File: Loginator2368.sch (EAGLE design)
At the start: 69 parts, among them J001 USBSMD, J002 M01PTH, J301 JST 2mm, J401 M06, J402 M04, J403 M10, J404 M06, J406 M12PTH, J701 MICROSD-SOCKET, Q050 PMOS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

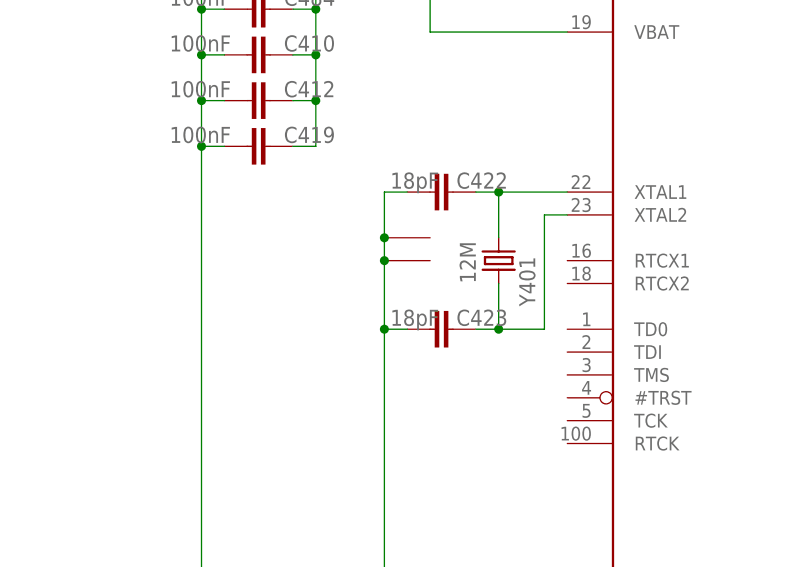
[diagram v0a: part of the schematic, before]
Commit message: Merged Mio's KwanSystems.lbr, updated all eagle files to use it.
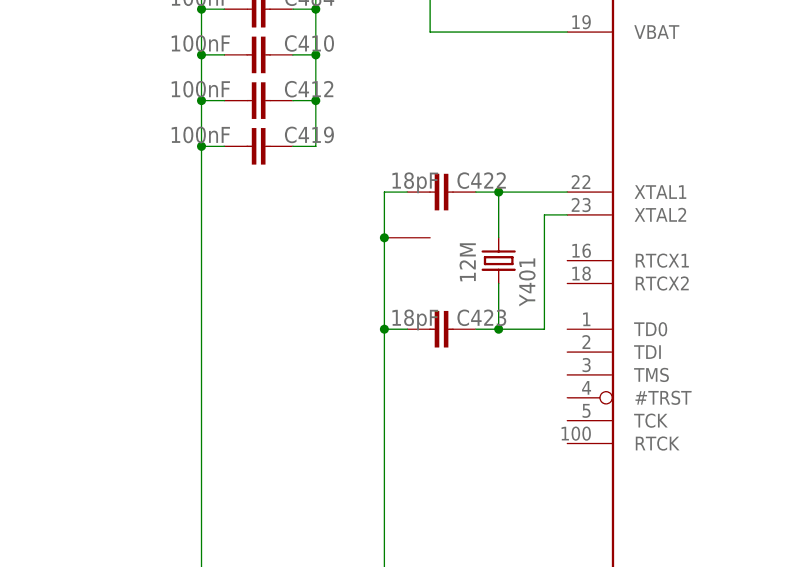
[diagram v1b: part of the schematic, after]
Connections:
- net GND: no longer Y401G$2.1
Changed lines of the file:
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@@
 <?xml version="1.0" encoding="utf-8"?>
 <!DOCTYPE eagle SYSTEM "eagle.dtd">
-<eagle version="6.1">
+<eagle version="6.2">
 <drawing>
 <settings>
@@
 <attribute name="DIGIKEY" value="887-1316-1-ND" x="-233.68" y="220.98" size="1.778" layer="96" rot="R90" display="off"/>
 </instance>
-<instance part="Y401" gate="G$2" x="-233.68" y="218.44" rot="R270"/>
 <instance part="Y401" gate="_" x="-220.98" y="218.44" smashed="yes" rot="R90">
 <attribute name="PART" x="-216.916" y="213.36" size="1.778" layer="95" rot="R90"/>
@@
 <wire x1="-231.14" y1="226.06" x2="-233.68" y2="226.06" width="0.1524" layer="91"/>
 <wire x1="-233.68" y1="226.06" x2="-233.68" y2="220.98" width="0.1524" layer="91"/>
-<wire x1="-233.68" y1="220.98" x2="-233.68" y2="218.44" width="0.1524" layer="91"/>
-<wire x1="-233.68" y1="218.44" x2="-233.68" y2="210.82" width="0.1524" layer="91"/>
+<wire x1="-233.68" y1="220.98" x2="-233.68" y2="210.82" width="0.1524" layer="91"/>
 <wire x1="-231.14" y1="210.82" x2="-233.68" y2="210.82" width="0.1524" layer="91"/>
 <junction x="-233.68" y="210.82"/>
 <junction x="-233.68" y="220.98"/>
-<junction x="-233.68" y="218.44"/>
 <pinref part="C422" gate="G$1" pin="1"/>
 <pinref part="C423" gate="G$1" pin="1"/>
 <pinref part="Y401" gate="G$1" pin="1"/>
-<pinref part="Y401" gate="G$2" pin="1"/>
 <wire x1="-233.68" y1="210.82" x2="-233.68" y2="175.26" width="0.1524" layer="91"/>
 <junction x="-233.68" y="119.38"/>
